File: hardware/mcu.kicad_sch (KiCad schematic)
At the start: 26 parts, among them SW1 SW_Push, SW4 SW_Push, U1 STM32L072RBTx

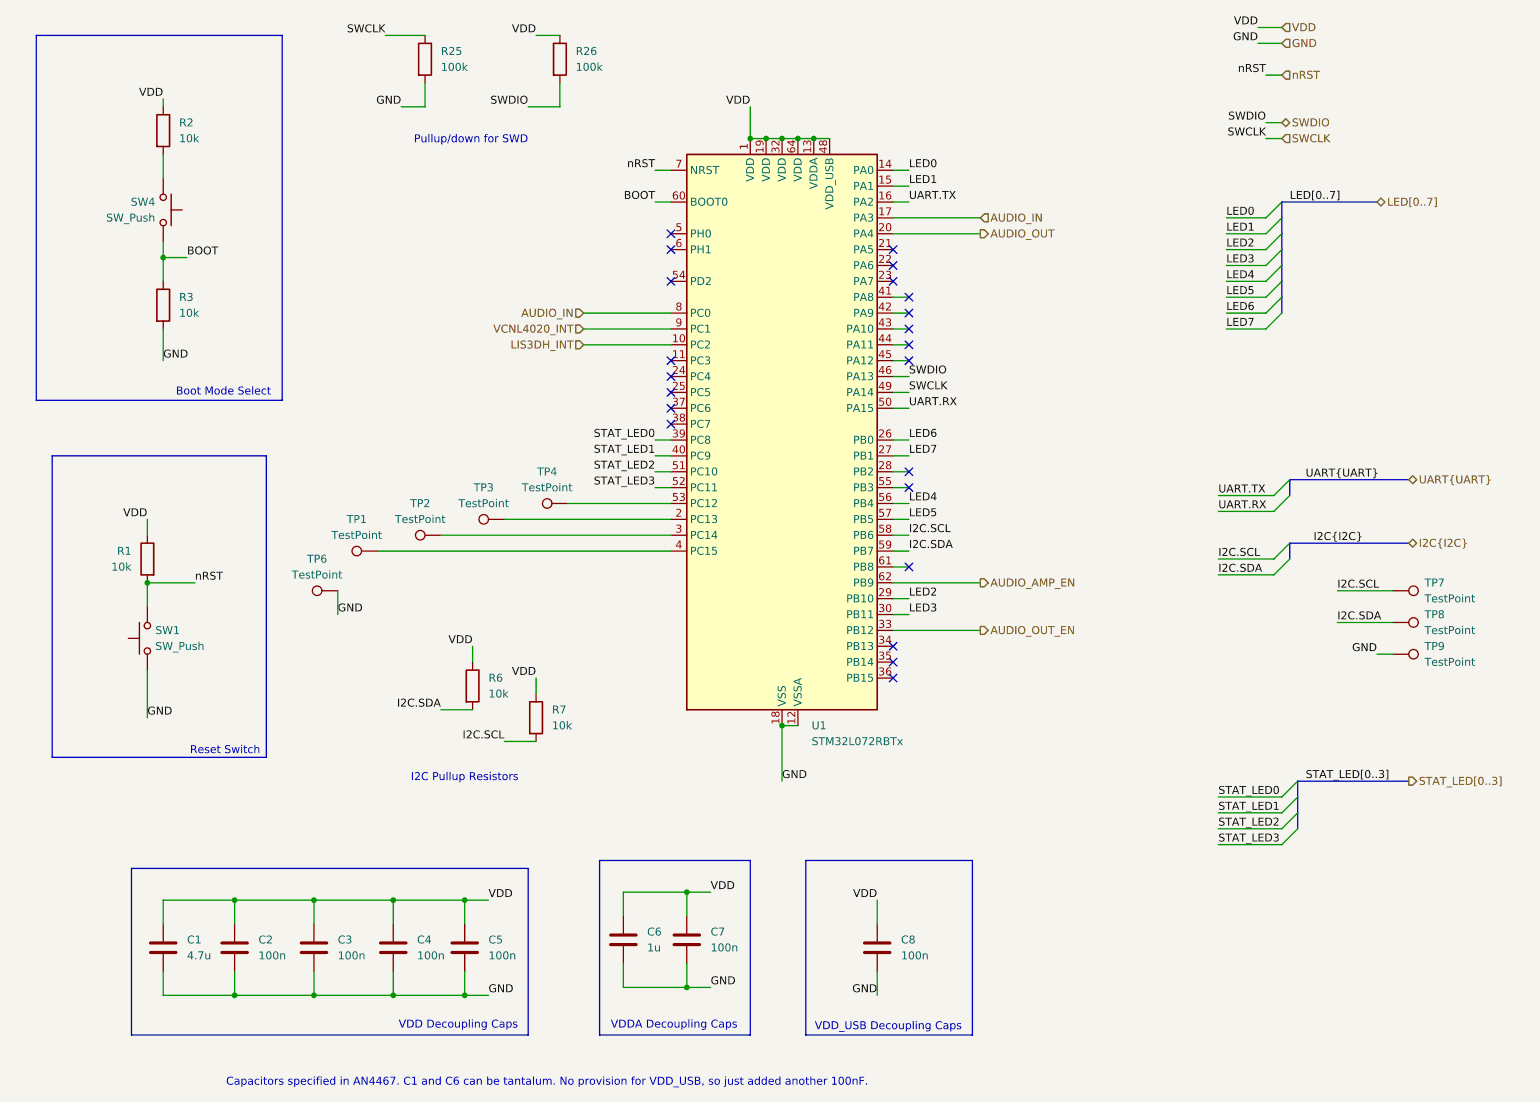
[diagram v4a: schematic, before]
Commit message: [Hardware] Update LEDs
Add additional LEDs and arrange in 7x7 matrix. Remove 2x status LEDs. Reroute MCU connetions to be more sensible. Rearrange components.
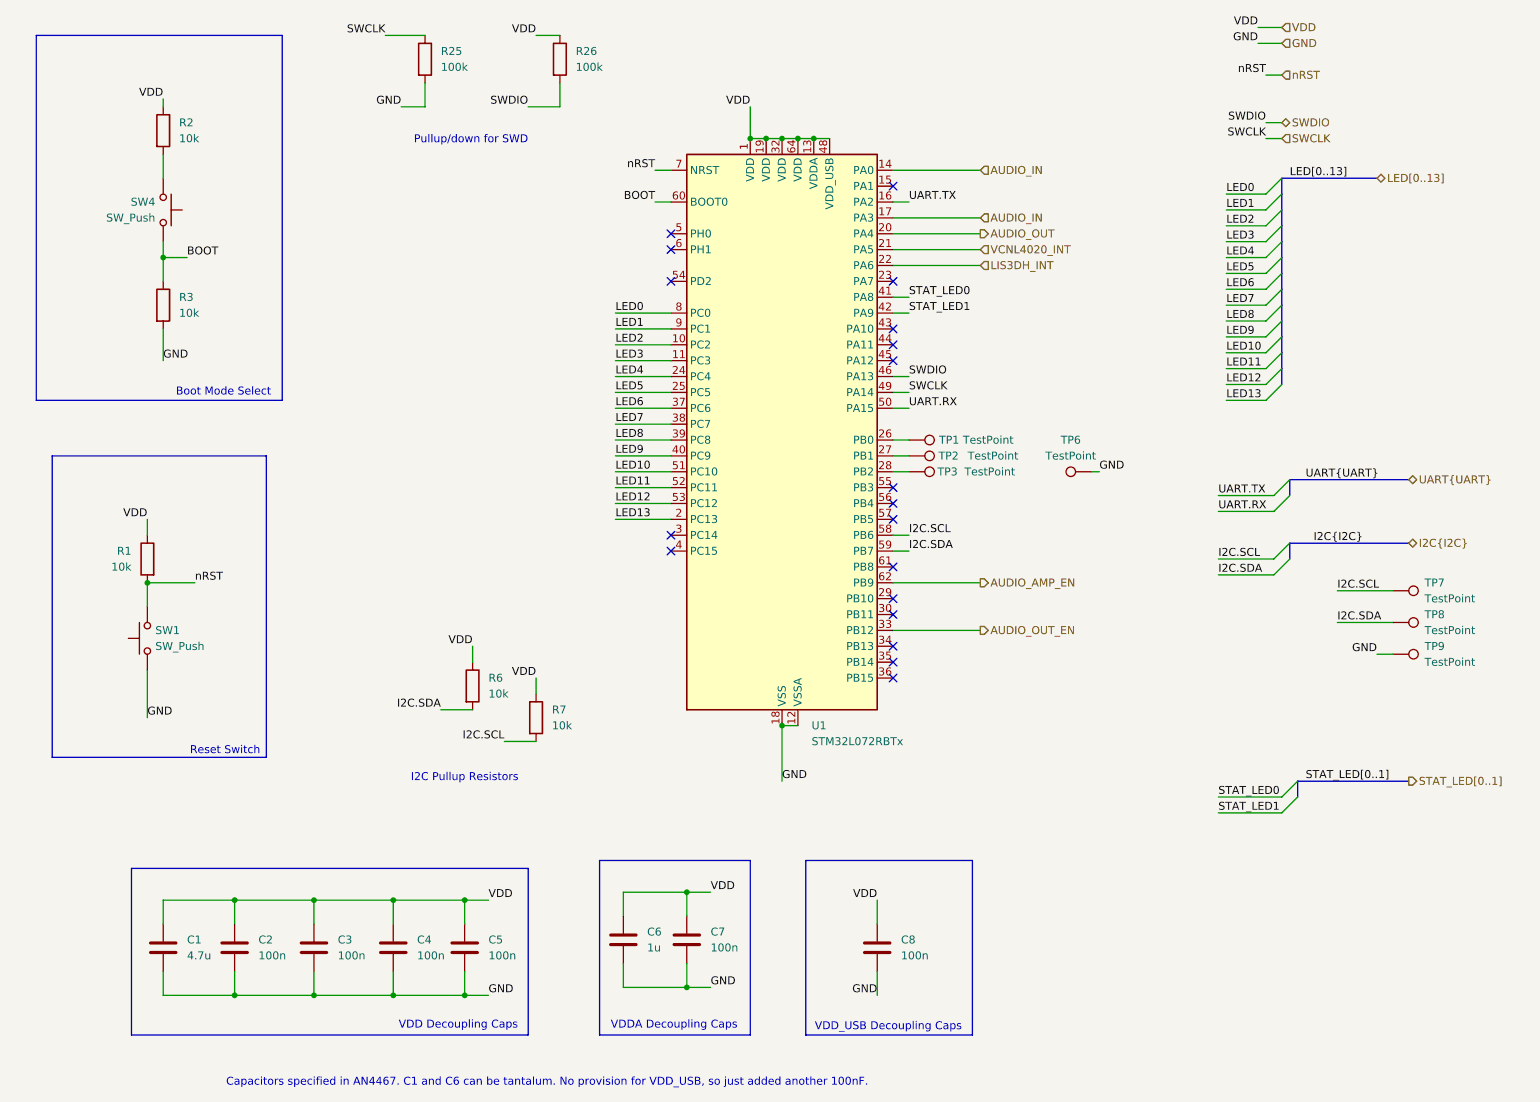
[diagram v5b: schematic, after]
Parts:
- removed TP4: TestPoint, Leaf_Jumper:TestPoint_0.5mm_1mm, symbol Connector:TestPoint
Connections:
- net AUDIO_IN: now also U1.14 (PA0); no longer U1.8 (PC0)
- net LED0: now also U1.8 (PC0); no longer U1.14 (PA0)
- net LED1: now also U1.9 (PC1); no longer U1.15 (PA1)
- net LED2: now also U1.10 (PC2); no longer U1.29 (PB10)
- net LED3: now also U1.11 (PC3); no longer U1.30 (PB11)
- net LED4: now also U1.24 (PC4); no longer U1.56 (PB4)
- net LED5: now also U1.25 (PC5); no longer U1.57 (PB5)
- net LED6: now also U1.37 (PC6); no longer U1.26 (PB0)
- net LED7: now also U1.38 (PC7); no longer U1.27 (PB1)
- net LIS3DH_INT: now also U1.22 (PA6); no longer U1.10 (PC2)
- net STAT_LED0: now also U1.41 (PA8); no longer U1.39 (PC8)
- net STAT_LED1: now also U1.42 (PA9); no longer U1.40 (PC9)
- net VCNL4020_INT: now also U1.21 (PA5); no longer U1.9 (PC1)
- net at TP3.1: now also U1.28 (PB2); no longer U1.2 (PC13)
- net at TP2.1: now also U1.27 (PB1); no longer U1.3 (PC14)
- net at TP1.1: now also U1.26 (PB0); no longer U1.4 (PC15)
- net LED12: now reaches U1.53 (PC12)
- net STAT_LED2 renamed LED10
- net STAT_LED3 renamed LED11
- new net LED13: U1.2 (PC13)
- new net LED8: U1.39 (PC8)
- new net LED9: U1.40 (PC9)
- no-connect marks 22 -> 19
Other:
- moved on the sheet: TP6

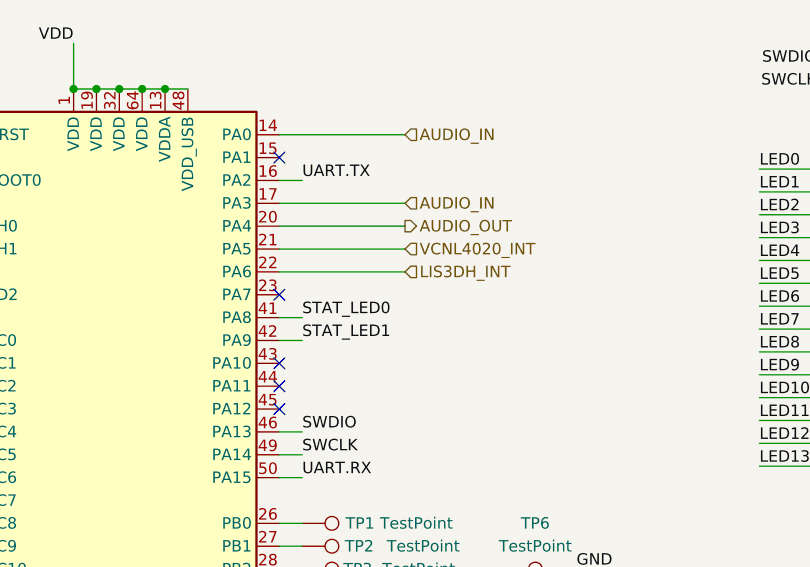
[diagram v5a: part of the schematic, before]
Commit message: [Hardware] Replace LISDH Motion Sensor with LSM6DSM
Change motion sensor to an accelerometer + gyro unit. Route the second interrupt line to the STM32.
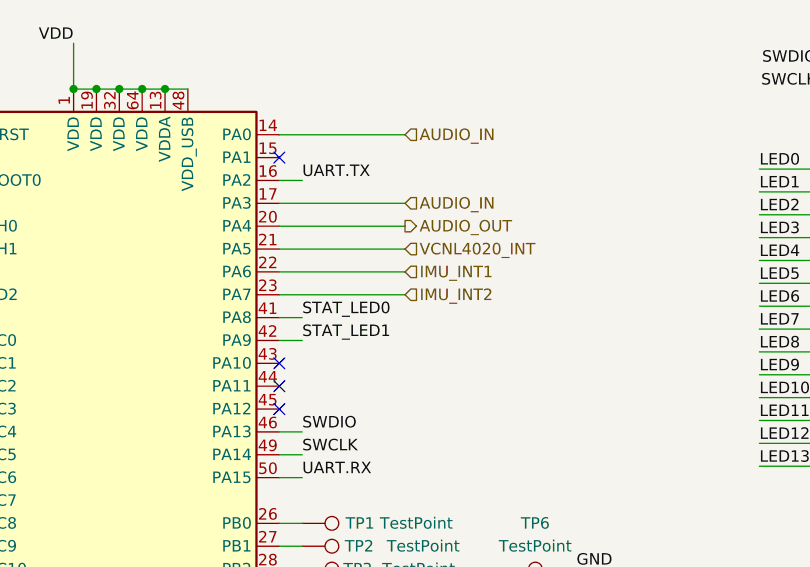
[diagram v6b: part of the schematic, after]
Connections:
- net IMU_INT2: now reaches U1.23 (PA7)
- net LIS3DH_INT renamed IMU_INT1
- no-connect marks 19 -> 18
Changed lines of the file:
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@@
-	)
-	(no_connect
-		(at 157.48 63.5)
 	)
 	(no_connect
@@
 	(wire
 		(pts
+			(xy 157.48 63.5) (xy 171.45 63.5)
+		)
+		(stroke
+			(width 0)
+			(type default)
+		)
+	)
+	(wire
+		(pts
 			(xy 154.94 162.56) (xy 154.94 166.37)
 		)
@@
 		)
 	)
-	(hierarchical_label "LIS3DH_INT"
+	(hierarchical_label "IMU_INT1"
 		(shape input)
 		(at 171.45 60.96 0)
@@
 		(fields_autoplaced yes)
 		(effects
+			(font
+				(size 1.27 1.27)
+			)
+			(justify left)
+		)
+	)
+	(hierarchical_label "IMU_INT2"
+		(shape input)
+		(at 171.45 63.5 0)
+		(fields_autoplaced yes)
+		(effects

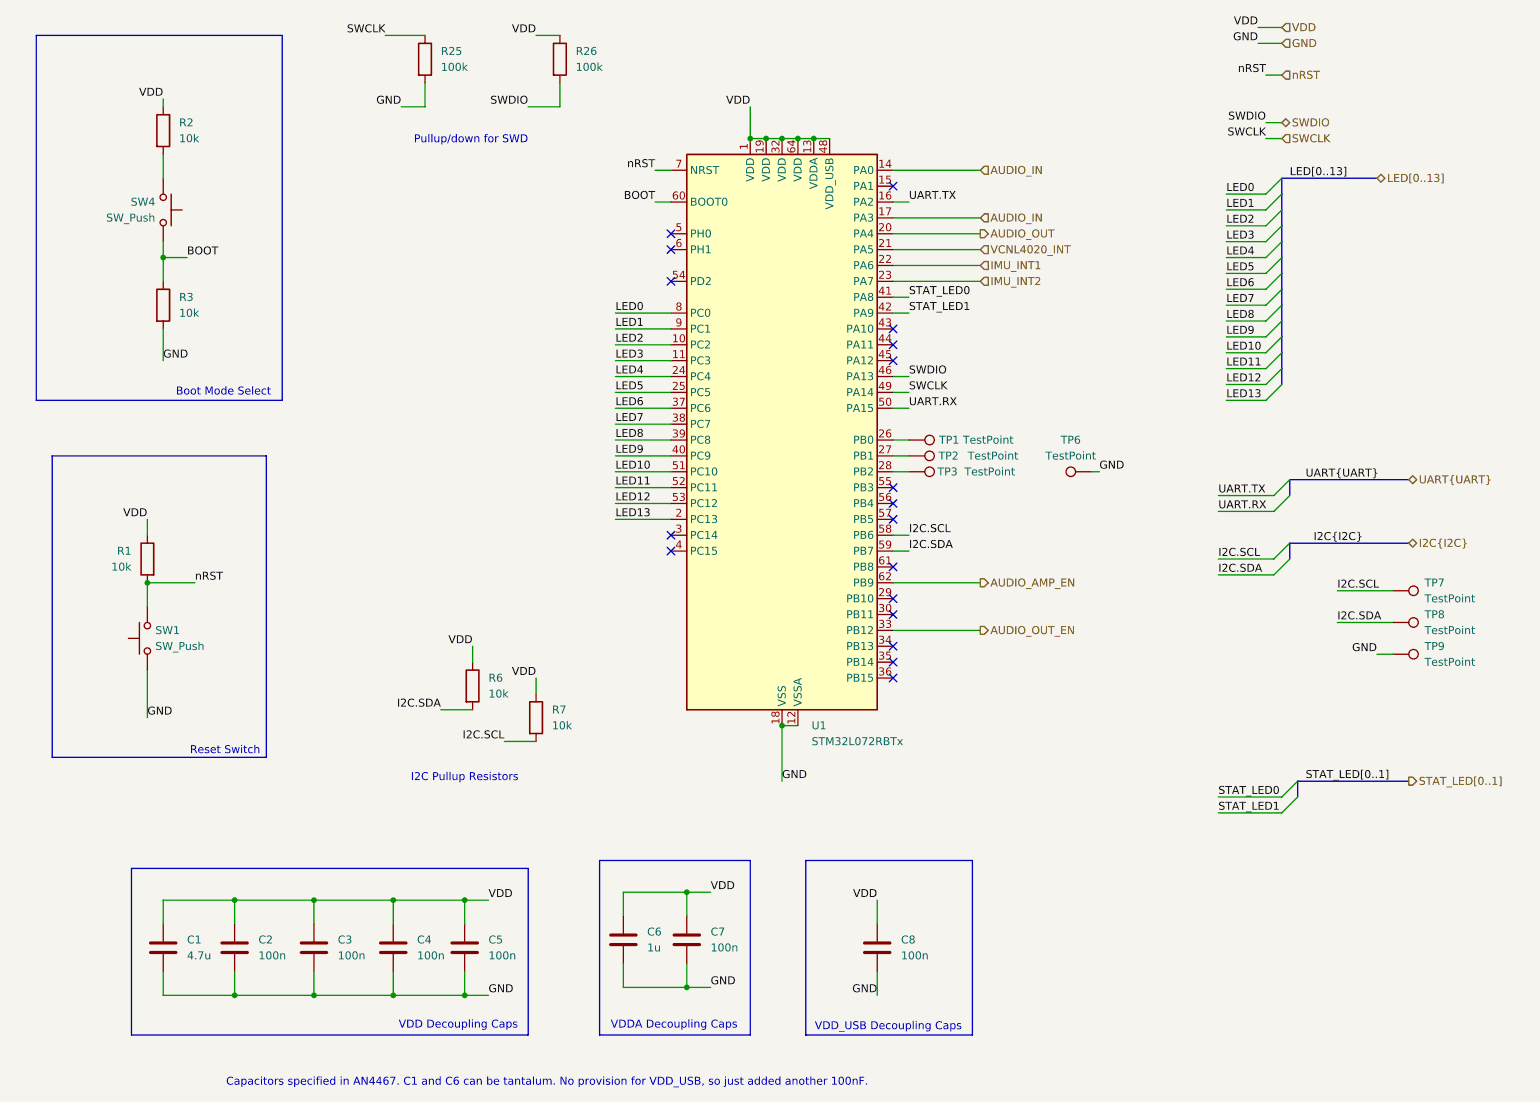
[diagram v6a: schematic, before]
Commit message: [Hardware] Add ferrite bead to VDDA. Swap schematic symbol for SWD-specific one. Add some notes to MCU pins.
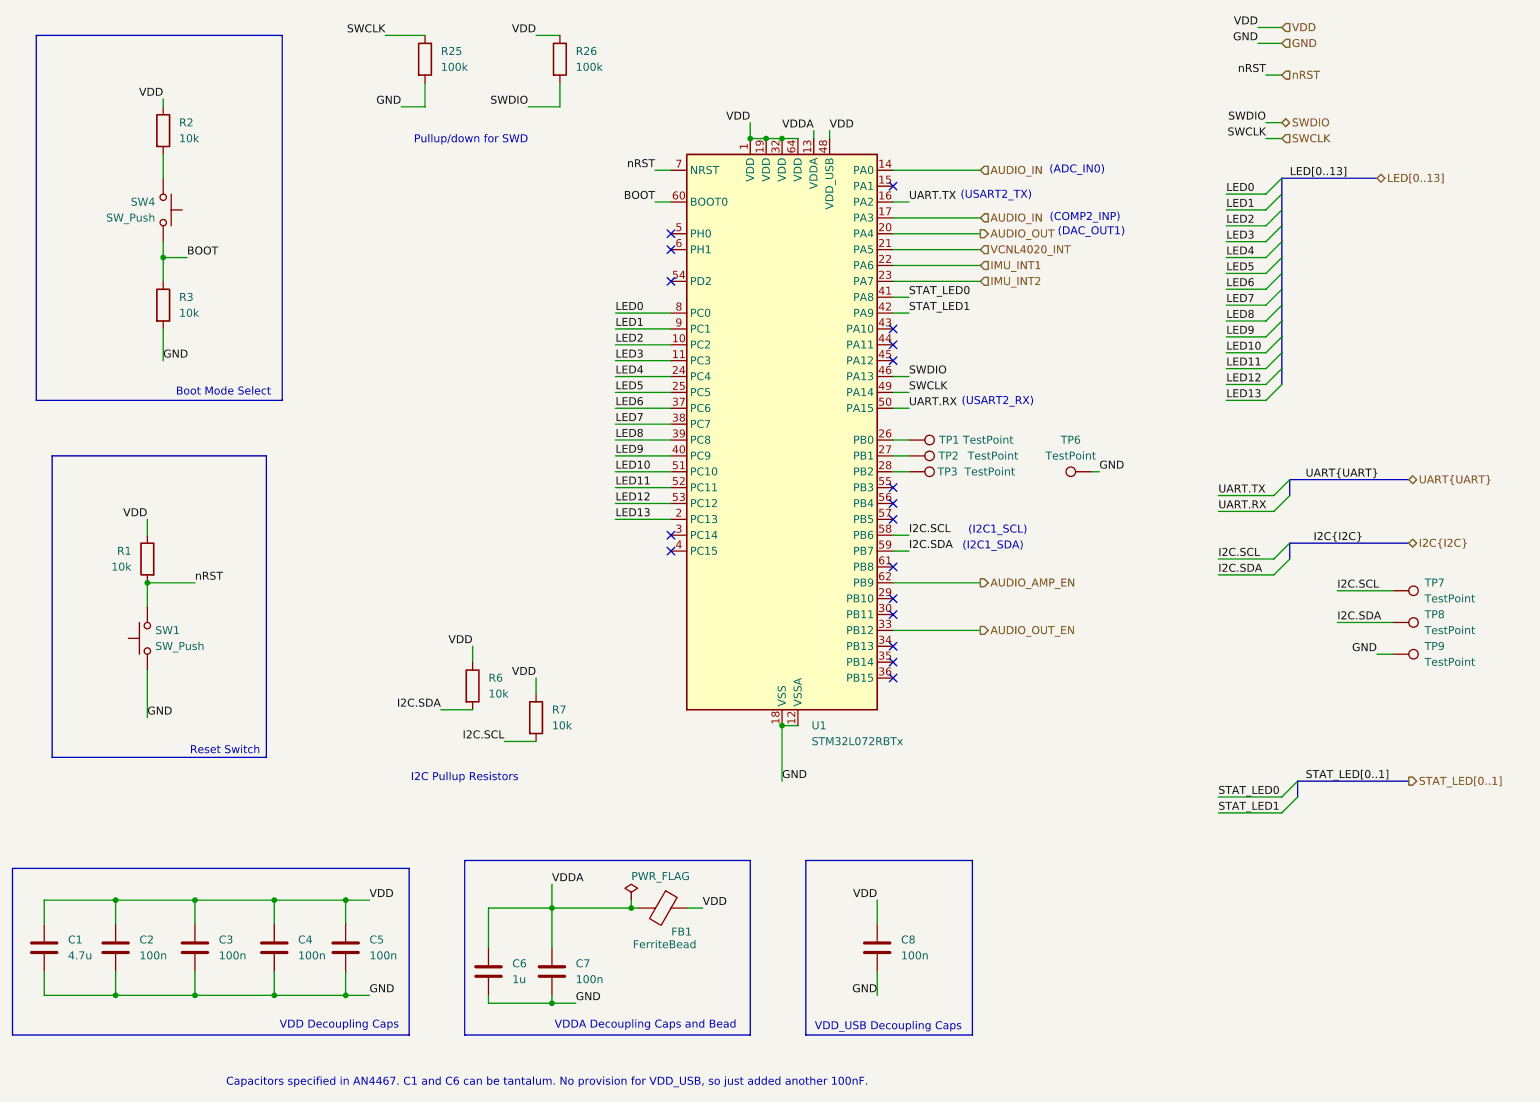
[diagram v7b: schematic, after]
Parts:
- added FB1: FerriteBead, Capacitor_SMD:C_0603_1608Metric_Pad1.08x0.95mm_HandSolder, symbol Device:FerriteBead
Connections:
- net VDD: now also FB1.1; no longer C6.1, C7.1, U1.13 (VDDA)
- new net VDDA: C6.1, C7.1, FB1.2, U1.13 (VDDA)
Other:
- note added: "(ADC_IN0)"
- note added: "(COMP2_INP)"
- note added: "(DAC_OUT1)"
- note added: "(I2C1_SCL)"
- note added: "(I2C1_SDA)"
- note added: "(USART2_RX)"
- note added: "(USART2_TX)"
- note added: "VDDA Decoupling Caps and Bead"
- note removed: "VDDA Decoupling Caps"
- moved on the sheet: C1, C2, C3, C4, C5, C6, C7

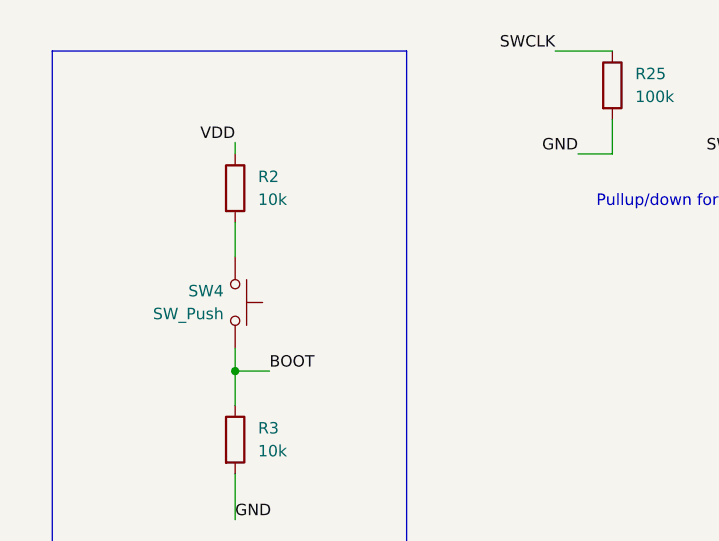
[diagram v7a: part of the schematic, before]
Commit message: [Hardware] Fix boot button pull-up resistor.
Had an extra resistor, remove it.
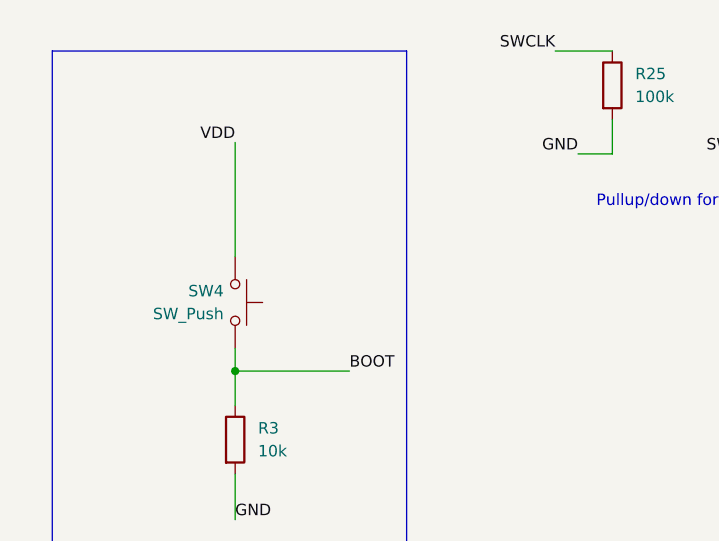
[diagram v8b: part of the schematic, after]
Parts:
- removed R2: 10k, Resistor_SMD:R_0603_1608Metric_Pad0.98x0.95mm_HandSolder, symbol Device:R
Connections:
- net VDD: now also SW4.2
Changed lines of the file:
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@@
 	(wire
 		(pts
+			(xy 40.64 34.29) (xy 40.64 46.99)
+		)
+		(stroke
+			(width 0)
+			(type default)
+		)
+	)
+	(wire
+		(pts
 			(xy 113.03 78.74) (xy 121.92 78.74)
 		)
@@
 	(wire
 		(pts
-			(xy 40.64 59.69) (xy 44.45 59.69)
+			(xy 40.64 59.69) (xy 53.34 59.69)
 		)
 		(stroke
@@
 	(wire
 		(pts
-			(xy 40.64 43.18) (xy 40.64 46.99)
-		)
-		(stroke
-			(width 0)
-			(type default)
-		)
-	)
-	(wire
-		(pts
 			(xy 228.6 118.11) (xy 237.49 118.11)
 		)
@@
 	(wire
 		(pts
-			(xy 40.64 34.29) (xy 40.64 35.56)
-		)
-		(stroke
-			(width 0)
-			(type default)
-		)
-	)
-	(wire
-		(pts
 			(xy 100.33 24.13) (xy 104.14 24.13)
 		)
@@
 		)
 	)
-	(label "BOOT"
-		(at 44.45 59.69 0)
-		(fields_autoplaced yes)
-		(effects
-			(font
-				(size 1.27 1.27)
-			)
-			(justify left bottom)
-		)
-	)
 	(label "VDD"
 		(at 38.1 101.6 180)
@@
 		)
 	)
+	(label "BOOT"
+		(at 53.34 59.69 0)
+		(fields_autoplaced yes)
+		(effects
+			(font
+				(size 1.27 1.27)
+			)
+			(justify left bottom)
+		)
+	)
 	(label "LED0"
 		(at 210.82 49.53 0)
@@
 					(unit 1)
 				)
-			)
-		)
-	)
-	(symbol
-		(lib_id "Device:R")
-		(at 40.64 39.37 0)
-		(unit 1)
-		(exclude_from_sim no)
-		(in_bom yes)
-		(on_board yes)
-		(dnp no)
-		(fields_autoplaced yes)
-		(property "Reference" "R2"
-			(at 43.18 38.0999 0)
-			(effects
-				(font
-					(size 1.27 1.27)
-				)
-				(justify left)
-			)
-		)
-		(property "Value" "10k"
-			(at 43.18 40.6399 0)
-			(effects
-				(font
-					(size 1.27 1.27)
-				)
-				(justify left)
-			)
-		)
-		(property "Footprint" "Resistor_SMD:R_0603_1608Metric_Pad0.98x0.95mm_HandSolder"
-			(at 38.862 39.37 90)
-			(effects
-				(font
-					(size 1.27 1.27)
-				)
-				(hide yes)
-			)
-		)
-		(property "Datasheet" "~"
-			(at 40.64 39.37 0)
-			(effects
-				(font
-					(size 1.27 1.27)
-				)
-				(hide yes)
-			)
-		)
-		(property "Description" "Resistor"
-			(at 40.64 39.37 0)
-			(effects
-				(font
-					(size 1.27 1.27)
-				)
-				(hide yes)
-			)
-		)
-		(pin "2"
-		)
-		(pin "1"
-		)
-		(instances
-			(project "holiday-widget"
-				(path "/addc3208-a9c4-4d28-9808-559c1d81e43b/1bdd200c-4b98-4ea0-bb61-84c7df1a198f"
-					(reference "R2")
-					(unit 1)
-				)
